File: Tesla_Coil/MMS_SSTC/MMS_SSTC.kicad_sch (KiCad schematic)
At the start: 48 parts, among them J1 Screw_Terminal_01x02, J2 Screw_Terminal_01x02, J3 Screw_Terminal_01x02, J4 Conn_01x01_Socket, Q1 IRFP460APBF, U1 NE555P, U3 LM7812_TO220, U4 CD74HC14E, U5 LM7805_TO220, U6 UCC27524P

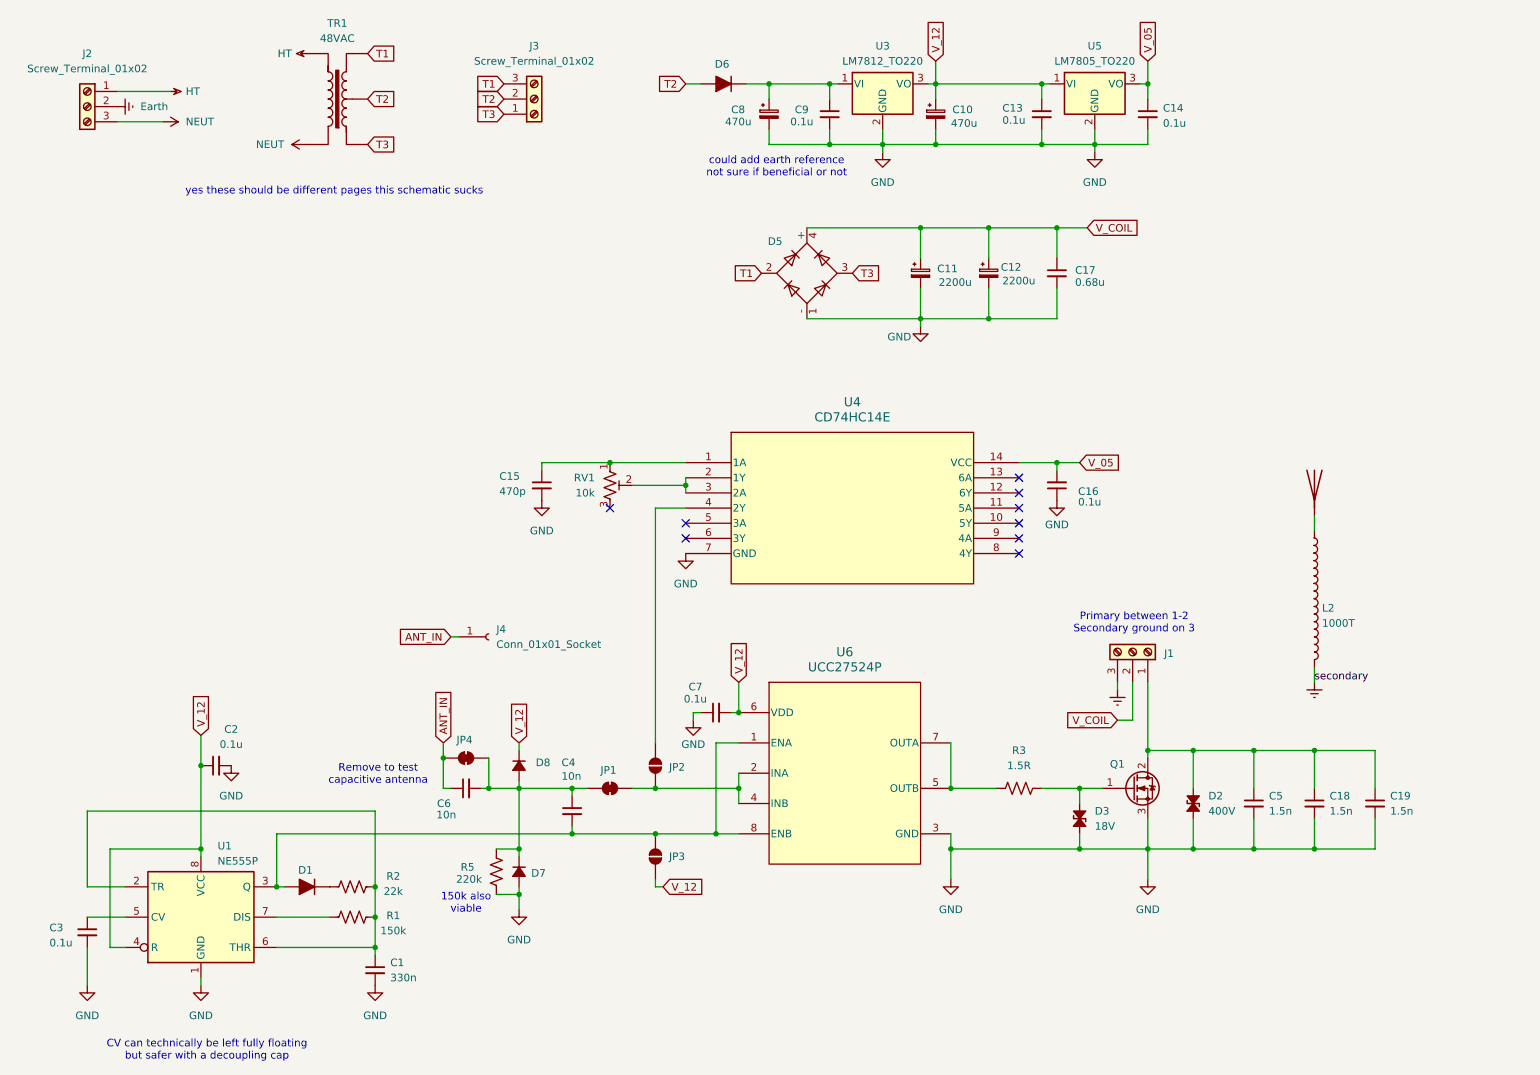
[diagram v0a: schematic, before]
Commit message: Begin work on SSTC prototype PCB
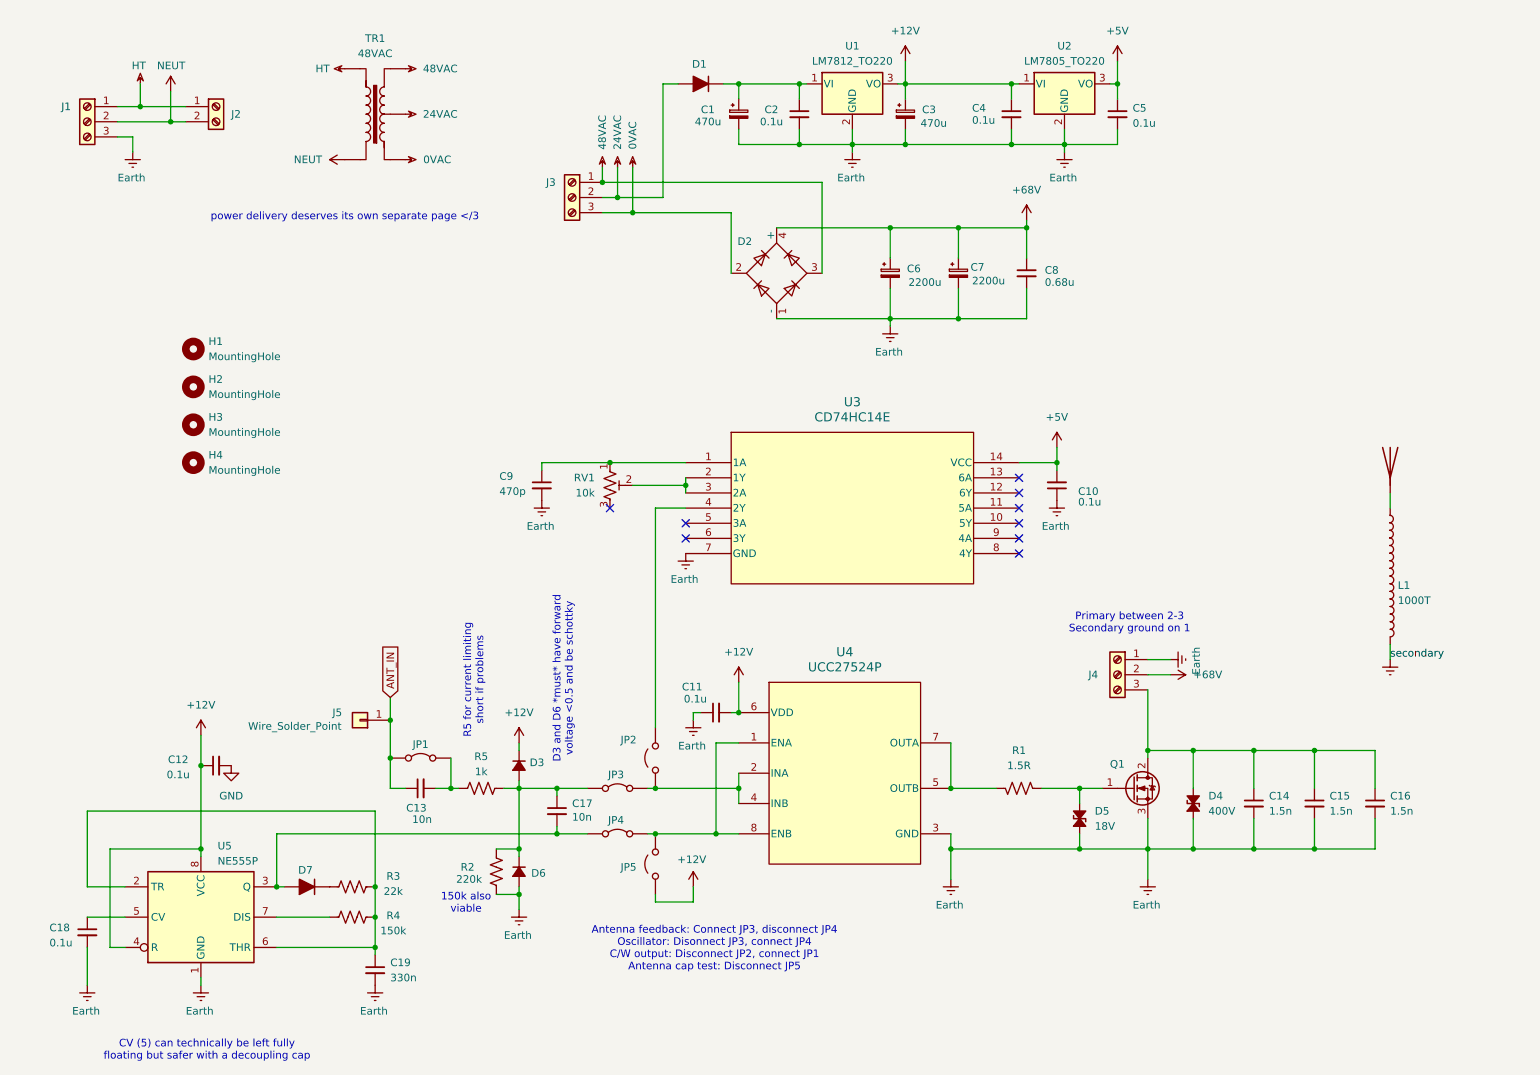
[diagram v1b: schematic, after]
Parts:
- removed J4: Conn_01x01_Socket, TestPoint:TestPoint_Keystone_5005-5009_Compact, symbol Connector:Conn_01x01_Socket
- removed JP1, JP4: SolderJumper_2_Bridged, Jumper:SolderJumper-2_P1.3mm_Open_RoundedPad1.0x1.5mm, symbol Jumper:SolderJumper_2_Bridged
- removed JP2, JP3: SolderJumper_2_Open, Jumper:SolderJumper-2_P1.3mm_Open_RoundedPad1.0x1.5mm, symbol Jumper:SolderJumper_2_Open
- added H1, H2, H3, H4: MountingHole, MountingHole:MountingHole_3.2mm_M3, symbol Mechanical:MountingHole
- added J2: Screw_Terminal_01x02, locals:691137710002, symbol Connector:Screw_Terminal_01x02
- added J5: Wire_Solder_Point, TestPoint:TestPoint_Keystone_5000-5004_Miniature, symbol Connector_Generic:Conn_01x01
- added JP1, JP3, JP4: Jumper_2_Bridged, TestPoint:TestPoint_Bridge_Pitch2.54mm_Drill0.7mm, symbol Jumper:Jumper_2_Bridged
- added JP2, JP5: Jumper_2_Open, TestPoint:TestPoint_Bridge_Pitch2.54mm_Drill0.7mm, symbol Jumper:Jumper_2_Open
- added R5: 1k, Resistor_THT:R_Axial_DIN0204_L3.6mm_D1.6mm_P5.08mm_Horizontal, symbol Device:R_US
- D1: renamed from D6; footprint Diode_THT:D_DO-201AD_P12.70mm_Horizontal -> Diode_THT:D_DO-41_SOD81_P7.62mm_Horizontal; DKPN 497-3216-1-ND -> 1N4004-TPMSCT-ND
- D3: renamed from D8; footprint Diode_THT:D_DO-201AD_P12.70mm_Horizontal -> Diode_THT:D_DO-41_SOD81_P7.62mm_Horizontal; DKPN 497-3216-1-ND -> 1N5817DICT-ND
- D6: renamed from D7; footprint Diode_THT:D_DO-201AD_P12.70mm_Horizontal -> Diode_THT:D_DO-41_SOD81_P7.62mm_Horizontal; DKPN 497-3216-1-ND -> 1N5817DICT-ND
- D7: renamed from D1; footprint Diode_THT:D_DO-201AD_P12.70mm_Horizontal -> Diode_THT:D_DO-41_SOD81_P7.62mm_Horizontal; DKPN 497-3216-1-ND -> 1N4004-TPMSCT-ND
- J1: renamed from J2; DKPN (none) -> 732-10956-ND
- J3: DKPN (none) -> 732-10956-ND
- J4: renamed from J1; DKPN (none) -> 732-10956-ND
- renumbered C8 to C1, C16 to C10, C7 to C11, C2 to C12, C6 to C13, C5 to C14, C18 to C15, C19 to C16, C4 to C17, C3 to C18, C1 to C19, C9 to C2, C10 to C3, C13 to C4, C14 to C5, C11 to C6, C12 to C7, C17 to C8, C15 to C9, D5 to D2, D2 to D4, D3 to D5, L2 to L1, R3 to R1, R5 to R2, R2 to R3, R1 to R4, U3 to U1, U5 to U2, U4 to U3, U6 to U4, U1 to U5
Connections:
- net ANT_IN: now also J5.1 (Pin_1), JP1.1 (A)
- net Earth: now also C1.2, C10.1, C11.1, C14.2, C15.2, C16.2, C18.2, C19.2, C2.2, C3.2, C4.2, C5.2, C6.2, C7.2, C8.2, C9.2, D2.1 (-), D4.1 (A1), D5.1 (A1), D6.2 (A), J1.3 (Pin_3), J4.1 (Pin_1), Q1.3 (S), R2.1, U1.2 (GND), U2.2 (GND), U3.7 (GND), U4.3 (GND), U5.1 (GND); no longer J1.2 (Pin_2), J4.3 (Pin_3)
- net GND: no longer C1.2, C10.1, C11.1, C14.2, C15.2, C16.2, C18.2, C19.2, C2.2, C3.2, C4.2, C5.2, C6.2, C7.2, C8.2, C9.2, D2.1 (-), D4.1 (A1), D5.1 (A1), D6.2 (A), Q1.3 (S), R2.1, U1.2 (GND), U2.2 (GND), U3.7 (GND), U4.3 (GND), U5.1 (GND)
- net HT: now also J2.1 (Pin_1)
- net NEUT: now also J1.2 (Pin_2), J2.2 (Pin_2); no longer J1.3 (Pin_3)
- net at C17.1, D3.2 (A), D6.1 (K)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: now also JP3.1 (A), R5.2; no longer C13.2
- net at C17.2, D7.2 (A), U5.3 (Q): now also JP4.1 (A); no longer U4.1 (ENA), U4.8 (ENB)
- net at U4.2 (INA), U4.4 (INB): now also JP2.1 (A), JP3.2 (B)
- net at U4.5 (OUTB), U4.7 (OUTA): now also R1.2; no longer R1.1
- net at C14.1, C15.1, C16.1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: now also J4.3 (Pin_3); no longer J4.1 (Pin_1)
- net at U3.4 (2Y): now also JP2.2 (B)
- net at D5.2 (A2), Q1.1 (G): now also R1.1; no longer R1.2
- net T1 renamed 0VAC
- net 0VAC: now also TR1.1; no longer TR1.3
- net T2 renamed 24VAC
- net T3 renamed 48VAC
- net 48VAC: now also TR1.3; no longer TR1.1
- net V_05 renamed +5V
- net V_12 renamed +12V
- net +12V: now also JP5.1 (A)
- net V_COIL renamed +68V
- new net: C13.2, JP1.2 (B), R5.1
- new net: JP4.2 (B), JP5.2 (B), U4.1 (ENA), U4.8 (ENB)
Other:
- note added: "Antenna feedback: Connect JP3, disconnect JP4 Oscillator: Disonnect JP3, connect JP4 C/W output: Disconnect JP2, connect JP1 Antenna cap test: Disconnect JP5"
- note added: "CV (5) can technically be left fully floating but safer with a decoupling cap"
- note added: "D3 and D6 *must* have forward voltage <0.5 and be schottky"
- note added: "Primary between 2-3 Secondary ground on 1"
- note added: "R5 for current limiting short if problems"
- note added: "power delivery deserves its own separate page </3"
- note removed: "CV can technically be left fully floating but safer with a decoupling cap"
- note removed: "Primary between 1-2 Secondary ground on 3"
- note removed: "Remove to test capacitive antenna"
- note removed: "could add earth reference not sure if beneficial or not"
- note removed: "yes these should be different pages this schematic sucks"
- moved on the sheet: C1, C13, C17, C2, C3, C4, C5, C6, C7, C8, D1, D2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

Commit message: Finish SSTC prototype PCB
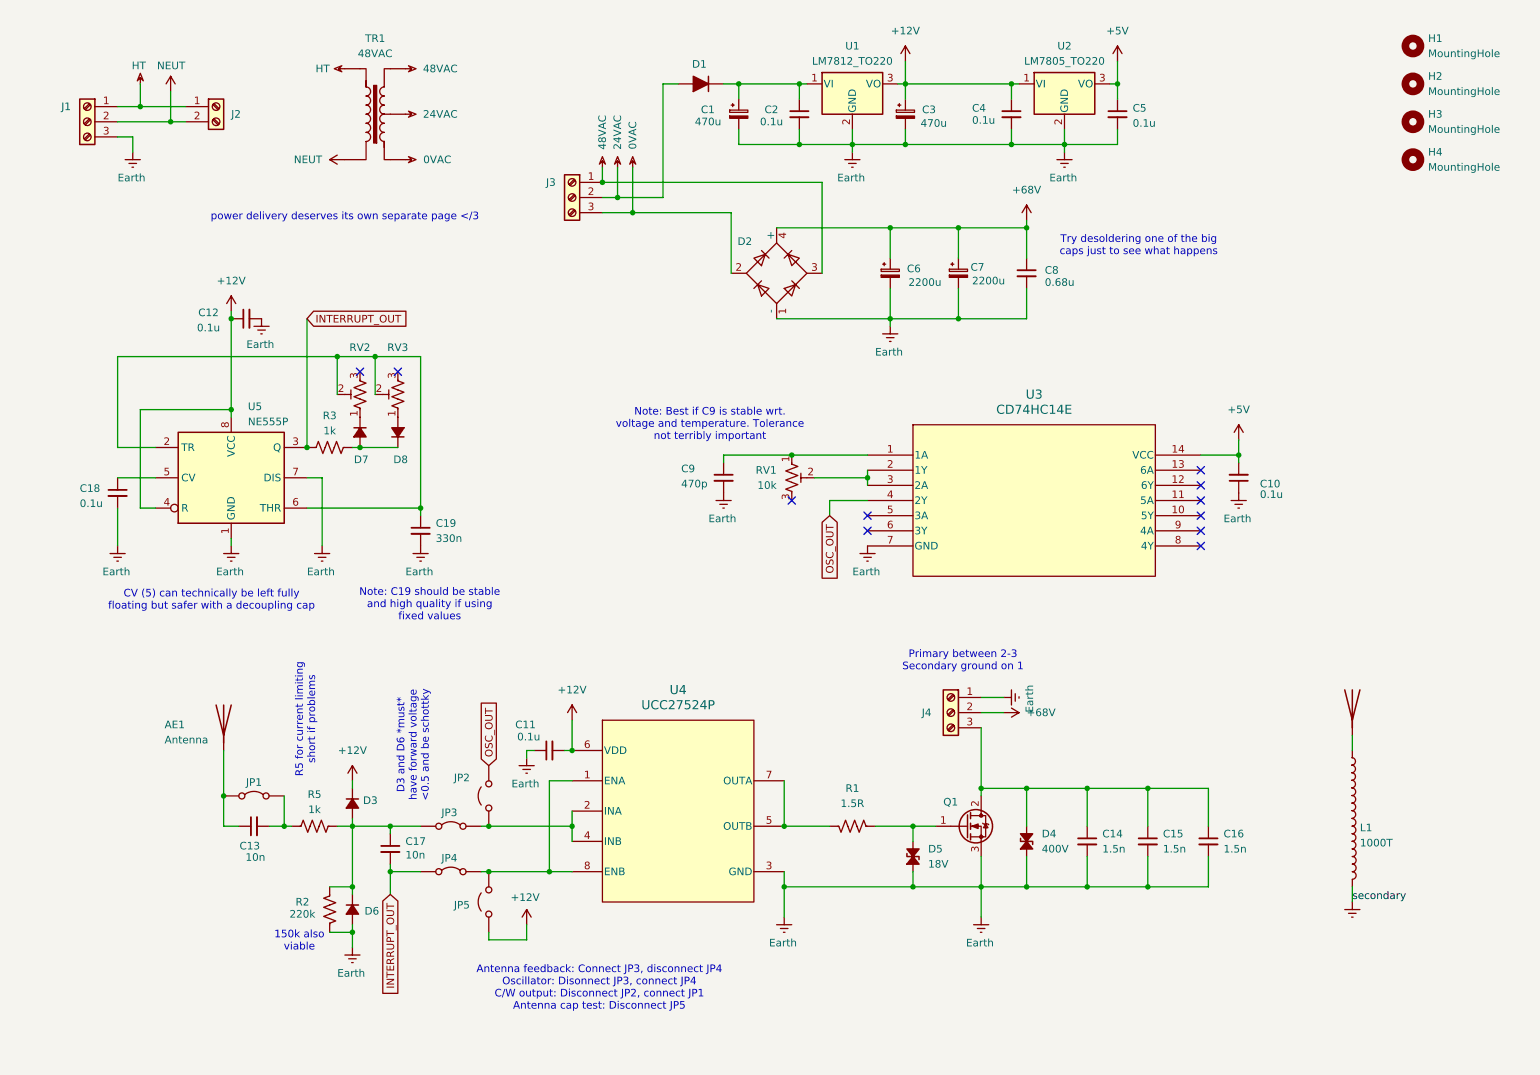
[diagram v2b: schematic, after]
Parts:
- removed D7: D_Filled, Diode_THT:D_DO-41_SOD81_P7.62mm_Horizontal, symbol Device:D_Filled
- removed J5: Wire_Solder_Point, TestPoint:TestPoint_Keystone_5000-5004_Miniature, symbol Connector_Generic:Conn_01x01
- removed R4: 150k, Resistor_THT:R_Axial_DIN0204_L3.6mm_D1.6mm_P5.08mm_Horizontal, symbol Device:R_US
- added AE1: Antenna, TestPoint:TestPoint_Keystone_5000-5004_Miniature, symbol Device:Antenna
- added D7, D8: D_Small_Filled, Diode_THT:D_DO-41_SOD81_P7.62mm_Horizontal, symbol Device:D_Small_Filled
- added RV2, RV3: R_Potentiometer_Trim_US, Potentiometer_THT:Potentiometer_Bourns_3296W_Vertical, symbol Device:R_Potentiometer_Trim_US
- C19: footprint Capacitor_THT:C_Disc_D5.1mm_W3.2mm_P5.00mm -> Capacitor_THT:C_Rect_L7.2mm_W3.5mm_P5.00mm_FKS2_FKP2_MKS2_MKP2; DKPN 478-10737-1-ND -> 399-R82DC3330SH60JCT-ND
- C9: footprint Capacitor_THT:C_Disc_D4.7mm_W2.5mm_P5.00mm -> Capacitor_THT:C_Rect_L7.2mm_W4.5mm_P5.00mm_FKS2_FKP2_MKS2_MKP2; DKPN BC2681CT-ND -> 1928-1270-ND
- R3: value 22k -> 1k; DKPN 56-MBA02040C2202FRP00CT-ND -> BC1.00KXCT-ND
- U3: footprint N14 -> Package_DIP:DIP-14_W7.62mm
- U4: footprint P0008A -> Package_DIP:DIP-8_W7.62mm
- renumbered AE1 to AE2
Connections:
- net GND is gone; now on net Earth: C12.2
- net Earth: now also U5.7 (DIS)
- net at C19.1, U5.2 (TR), U5.6 (THR): now also RV2.2, RV3.2; no longer R3.2
- net OSC_OUT: now reaches JP2.2 (B), U3.4 (2Y)
- net INTERRUPT_OUT: now reaches R3.1
- net INTERRUPT_OUT: now also C17.2, JP4.1 (A), U5.3 (Q)
- net ANT_IN: no longer names the net of C13.1, JP1.1 (A)
- net ANT_IN: now also AE1.1 (A)
- new net: D7.2 (A), D8.1 (K), R3.2
- new net: D8.2 (A), RV3.1
- new net: D7.1 (K), RV2.1
- no-connect marks 9 -> 11
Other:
- note added: "Note: Best if C9 is stable wrt. voltage and temperature. Tolerance not terribly important"
- note added: "Note: C19 should be stable and high quality if using fixed values"
- note added: "Try desoldering one of the big caps just to see what happens"
- moved on the sheet: C10, C11, C12, C13, C14, C15, C16, C17, C18, C19, C9, D3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

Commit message: Commit minor changes to SSTC
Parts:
- RV1: footprint Potentiometer_THT:Potentiometer_Bourns_3296X_Horizontal -> Potentiometer_THT:Potentiometer_Bourns_3296W_Vertical; DKPN 3296X-103LF-ND -> 118-3296W-1-103RLFCT-ND
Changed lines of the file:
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@@
 			)
 		)
-		(property "Footprint" "Potentiometer_THT:Potentiometer_Bourns_3296X_Horizontal"
+		(property "Footprint" "Potentiometer_THT:Potentiometer_Bourns_3296W_Vertical"
 			(at 143.51 91.44 0)
 			(effects
@@
 			)
 		)
-		(property "DKPN" "3296X-103LF-ND"
+		(property "DKPN" "118-3296W-1-103RLFCT-ND"
 			(at 143.51 91.44 0)
 			(effects

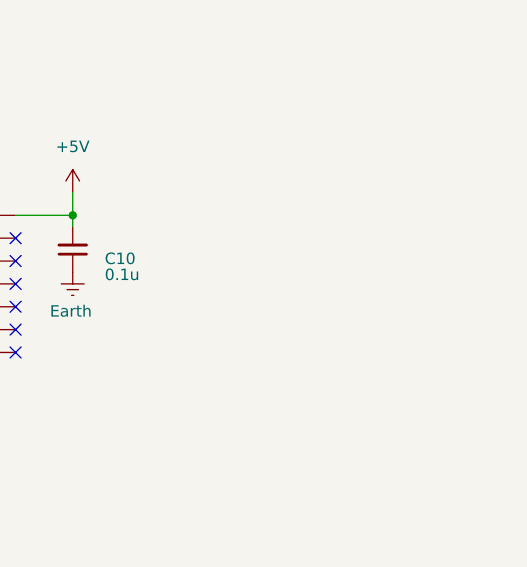
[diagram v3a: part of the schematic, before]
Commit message: Start work on SSTC power supply
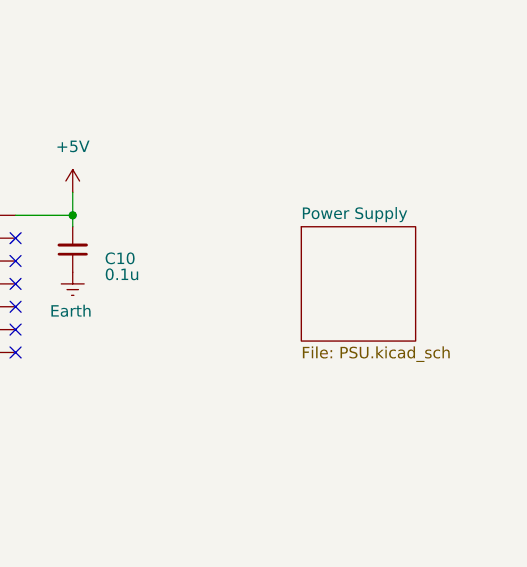
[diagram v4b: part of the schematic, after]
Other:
- added sheet Power Supply (PSU.kicad_sch)
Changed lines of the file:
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@@
+		)
+	)
+	(sheet
+		(at 243.84 88.9)
+		(size 12.7 12.7)
+		(exclude_from_sim no)
+		(in_bom yes)
+		(on_board yes)
+		(dnp no)
+		(fields_autoplaced yes)
+		(stroke
+			(width 0.1524)
+			(type solid)
+		)
+		(fill
+			(color 0 0 0 0.0000)
+		)
+		(property "Sheetname" "Power Supply"
+			(at 243.84 88.1884 0)
+			(effects
+				(font
+					(size 1.27 1.27)
+				)
+				(justify left bottom)
+			)
+		)
+		(property "Sheetfile" "PSU.kicad_sch"
+			(at 243.84 102.1846 0)
+			(effects
+				(font
+					(size 1.27 1.27)
+				)
+				(justify left top)
+			)
+		)
+		(instances
+			(project "MMS_SSTC"
+				(path "/b29a3901-c128-4c19-b69f-61de71283b43"
+					(page "2")
+				)
+			)
 		)
 	)
